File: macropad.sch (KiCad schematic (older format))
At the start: 13 parts, among them SW1 Rotary_Encoder_Switch, SW2 Rotary_Encoder_Switch, SW3 Rotary_Encoder_Switch, SW4 Rotary_Encoder_Switch, SW5 Rotary_Encoder_Switch, SW6 Rotary_Encoder_Switch, U1 ProMicro

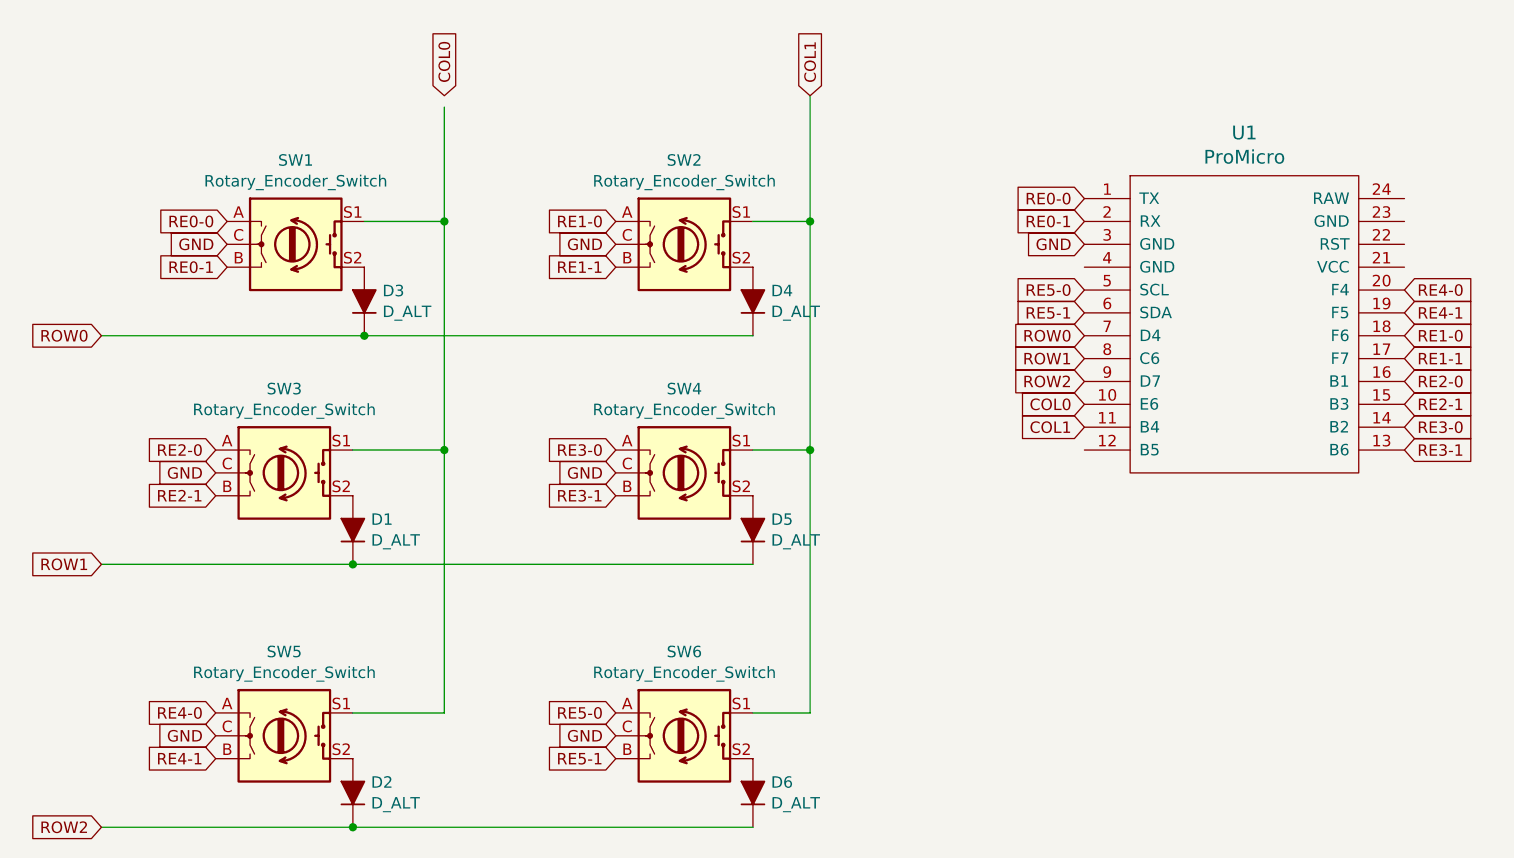
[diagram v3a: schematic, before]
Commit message: finished first pass routing
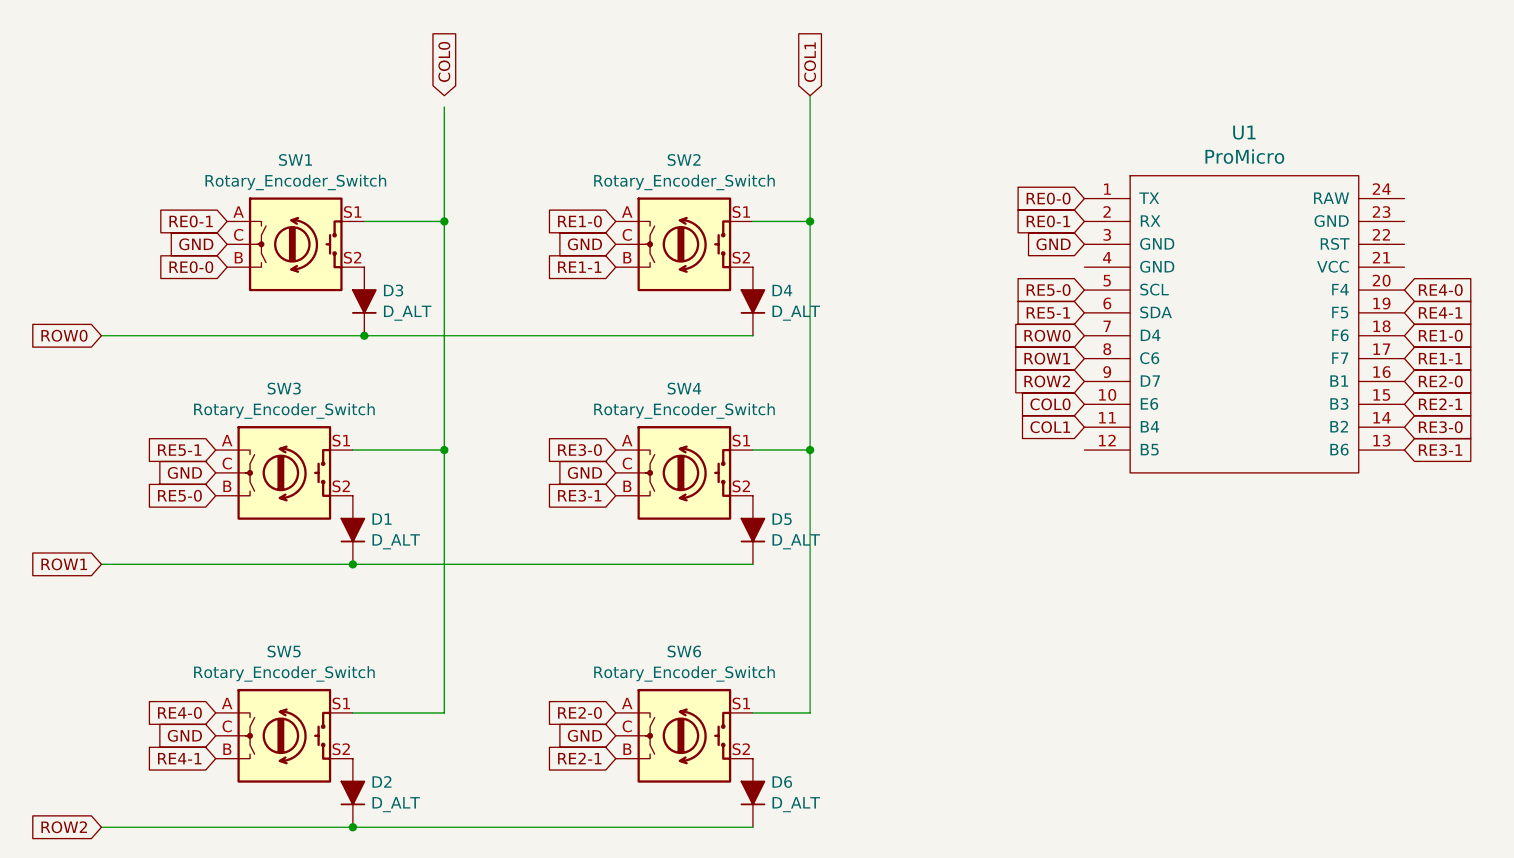
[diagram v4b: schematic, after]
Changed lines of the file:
@@
 Text GLabel 7100 3000 0    50   Input ~ 0
 COL1
+Text GLabel 3350 2300 0    50   Input ~ 0
+RE0-0
 Text GLabel 3350 2100 0    50   Input ~ 0
-RE0-0
-Text GLabel 3350 2300 0    50   Input ~ 0
 RE0-1
 Text GLabel 5050 2100 0    50   Input ~ 0
@@
 Text GLabel 5050 2300 0    50   Input ~ 0
 RE1-1
-Text GLabel 3300 3100 0    50   Input ~ 0
+Text GLabel 5050 4250 0    50   Input ~ 0
 RE2-0
-Text GLabel 3300 3300 0    50   Input ~ 0
+Text GLabel 5050 4450 0    50   Input ~ 0
 RE2-1
 Text GLabel 5050 3100 0    50   Input ~ 0
@@
 Text GLabel 3300 4450 0    50   Input ~ 0
 RE4-1
-Text GLabel 5050 4250 0    50   Input ~ 0
+Text GLabel 3300 3300 0    50   Input ~ 0
 RE5-0
-Text GLabel 5050 4450 0    50   Input ~ 0
+Text GLabel 3300 3100 0    50   Input ~ 0
 RE5-1
 Text GLabel 7100 2000 0    50   Input ~ 0

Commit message: Created new footprint and fixed routing
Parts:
- SW1, SW2, SW3, SW4, SW5, SW6: footprint Keebio-Parts:RotaryEncoder_Alps_EC11E-Switch_Vertical_H20mm -> Rotary_Encoder:RotaryEncoder_MX
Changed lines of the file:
@@
 F 0 "SW1" H 3650 2567 50  0000 C CNN
 F 1 "Rotary_Encoder_Switch" H 3650 2476 50  0000 C CNN
-F 2 "Keebio-Parts:RotaryEncoder_Alps_EC11E-Switch_Vertical_H20mm" H 3500 2360 50  0001 C CNN
+F 2 "Rotary_Encoder:RotaryEncoder_MX" H 3500 2360 50  0001 C CNN
 F 3 "~" H 3650 2460 50  0001 C CNN
 	1    3650 2200
@@
 F 0 "SW3" H 3600 3567 50  0000 C CNN
 F 1 "Rotary_Encoder_Switch" H 3600 3476 50  0000 C CNN
-F 2 "Keebio-Parts:RotaryEncoder_Alps_EC11E-Switch_Vertical_H20mm" H 3450 3360 50  0001 C CNN
+F 2 "Rotary_Encoder:RotaryEncoder_MX" H 3450 3360 50  0001 C CNN
 F 3 "~" H 3600 3460 50  0001 C CNN
 	1    3600 3200
@@
 F 0 "SW5" H 3600 4717 50  0000 C CNN
 F 1 "Rotary_Encoder_Switch" H 3600 4626 50  0000 C CNN
-F 2 "Keebio-Parts:RotaryEncoder_Alps_EC11E-Switch_Vertical_H20mm" H 3450 4510 50  0001 C CNN
+F 2 "Rotary_Encoder:RotaryEncoder_MX" H 3450 4510 50  0001 C CNN
 F 3 "~" H 3600 4610 50  0001 C CNN
 	1    3600 4350
@@
 F 0 "SW2" H 5350 2567 50  0000 C CNN
 F 1 "Rotary_Encoder_Switch" H 5350 2476 50  0000 C CNN
-F 2 "Keebio-Parts:RotaryEncoder_Alps_EC11E-Switch_Vertical_H20mm" H 5200 2360 50  0001 C CNN
+F 2 "Rotary_Encoder:RotaryEncoder_MX" H 5200 2360 50  0001 C CNN
 F 3 "~" H 5350 2460 50  0001 C CNN
 	1    5350 2200
@@
 F 0 "SW4" H 5350 3567 50  0000 C CNN
 F 1 "Rotary_Encoder_Switch" H 5350 3476 50  0000 C CNN
-F 2 "Keebio-Parts:RotaryEncoder_Alps_EC11E-Switch_Vertical_H20mm" H 5200 3360 50  0001 C CNN
+F 2 "Rotary_Encoder:RotaryEncoder_MX" H 5200 3360 50  0001 C CNN
 F 3 "~" H 5350 3460 50  0001 C CNN
 	1    5350 3200
@@
 F 0 "SW6" H 5350 4717 50  0000 C CNN
 F 1 "Rotary_Encoder_Switch" H 5350 4626 50  0000 C CNN
-F 2 "Keebio-Parts:RotaryEncoder_Alps_EC11E-Switch_Vertical_H20mm" H 5200 4510 50  0001 C CNN
+F 2 "Rotary_Encoder:RotaryEncoder_MX" H 5200 4510 50  0001 C CNN
 F 3 "~" H 5350 4610 50  0001 C CNN
 	1    5350 4350
